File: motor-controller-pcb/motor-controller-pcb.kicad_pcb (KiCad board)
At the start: 2 copper layers, 90 x 65 mm, 15 parts, among them J1 Conn_01x06_Pin, J2 Conn_01x06_Pin, J3 Conn_01x06_Pin, J4 Conn_01x06_Pin, J5 Conn_01x04_Pin, J6 Conn_01x04_Pin, M1 Conn_01x02_Pin, M2 Conn_01x02_Pin, M3 Conn_01x02_Pin, M4 Conn_01x02_Pin

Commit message: fix: change pcb footprint to jst ph
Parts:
- J1, J2, J3, J4: footprint Connector_JST:JST_SH_BM06B-SRSS-TB_1x06-1MP_P1.00mm_Vertical -> Connector_JST:JST_PH_B6B-PH-K_1x06_P2.00mm_Vertical
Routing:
- net +5V: track 146.9 -> 0.00 mm
- net /Encoder 2A: track 79.7 -> 1.22 mm
- net /Encoder 1B: track 68.7 -> 1.13 mm, vias 2 -> 0
- net /Encoder 3B: track 50.0 -> 0.00 mm
- net GND: track 148.4 -> 100.4 mm, vias 3 -> 0
- net /Encoder 2B: track 47.4 -> 0.00 mm, vias 1 -> 0
- net /Encoder 3A: track 45.5 -> 0.00 mm
- net /Encoder 1A: track 45.4 -> 0.00 mm, vias 1 -> 0
- net Net-(J4-Pin_1): track 33.7 -> 0.00 mm
- net /Encoder 4B: track 33.7 -> 0.00 mm, vias 1 -> 0
- net /Encoder 4A: track 33.2 -> 0.00 mm, vias 1 -> 0
- net Net-(J2-Pin_1): track 29.8 -> 0.00 mm, vias 2 -> 0
- net Net-(J1-Pin_6): track 28.3 -> 0.00 mm, vias 1 -> 0
- net Net-(J4-Pin_6): track 22.0 -> 0.00 mm
- net Net-(J2-Pin_6): track 19.4 -> 0.00 mm
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
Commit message: feat: pcb layout
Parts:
- removed M1, M2, M3, M4: Conn_01x02_Pin, Connector_PinHeader_2.54mm:PinHeader_1x02_P2.54mm_Vertical
- removed REF** (x4): MountingHole_3.2mm_M3, MountingHole:MountingHole_3.2mm_M3
- added C1: 470uF, Capacitor_THT:CP_Radial_D8.0mm_P3.50mm, F.Cu at (115.6, 129.5)
- added C2: 100nF, Capacitor_SMD:C_0805_2012Metric, F.Cu at (146.1, 78.7)
- added C3: 100nF, Capacitor_SMD:C_0805_2012Metric, F.Cu at (146.1, 39.4)
- added C4: 100nF, Capacitor_SMD:C_0805_2012Metric, F.Cu at (180.3, 59.7)
- added F1: Fuse, Fuse:Fuseholder_Clip-5x20mm_Littelfuse_100_Inline_P20.50x4.60mm_D1.30mm_Horizontal, F.Cu at (152.4, 105.4)
- added J10: 3V3, Connector_PinHeader_2.54mm:PinHeader_1x10_P2.54mm_Vertical, F.Cu at (196.7, 67.3)
- added J11: Conn_01x05_Pin, Connector_PinHeader_2.54mm:PinHeader_1x05_P2.54mm_Vertical, F.Cu at (195.4, 97.8)
- added J7: GND, Connector_PinHeader_2.54mm:PinHeader_1x10_P2.54mm_Vertical, F.Cu at (182.9, 67.3)
- added J8: 5V, Connector_PinHeader_2.54mm:PinHeader_1x10_P2.54mm_Vertical, F.Cu at (187.5, 67.3)
- added J9: V_Batt, Connector_PinHeader_2.54mm:PinHeader_1x10_P2.54mm_Vertical, F.Cu at (192.1, 67.3)
- added SW1: Battery Switch, Connector_Wire:SolderWire-2sqmm_1x02_P7.8mm_D2mm_OD3.9mm_Relief2x, F.Cu at (125.7, 140.0)
- added TP1: 5V TestPoint, TestPoint:TestPoint_Pad_1.5x1.5mm, F.Cu at (181.6, 106.7)
- added TP2: GND TestPoint, TestPoint:TestPoint_Pad_1.5x1.5mm, F.Cu at (186.7, 106.7)
- added TP3: V_Batt Test Point, TestPoint:TestPoint_Pad_1.5x1.5mm, F.Cu at (191.5, 106.7)
- added TP4: 3V3 Test Point, TestPoint:TestPoint_Pad_1.5x1.5mm, F.Cu at (196.8, 106.7)
- added U1: ~, robocup-library:DRI044, F.Cu at (137.2, 88.9)
- added U2: ~, robocup-library:DRI044, F.Cu at (137.2, 49.5)
- added U3: ~, robocup-library:DRI044, F.Cu at (189.2, 49.5)
- J1: value Conn_01x06_Pin -> Motor 1
- J2: value Conn_01x06_Pin -> Motor 2
- J3: value Conn_01x06_Pin -> Motor 3
- J4: value Conn_01x06_Pin -> Motor 4
- J5: value Conn_01x04_Pin -> Dribbler Motor; footprint Connector_PinHeader_2.54mm:PinHeader_1x04_P2.54mm_Vertical -> Connector_JST:JST_PH_B6B-PH-K_1x06_P2.00mm_Vertical
- J6: value Conn_01x04_Pin -> Battery Connector; footprint Connector_PinHeader_2.54mm:PinHeader_1x04_P2.54mm_Vertical -> Connector_Wire:SolderWire-2sqmm_1x02_P7.8mm_D2mm_OD3.9mm_Relief2x
- moved J3 115.4 mm to (212.1, 43.3), turned to -90 degrees
- moved J2 79.2 mm to (115.6, 53.2), turned to 90 degrees
- moved J6 47.2 mm to (125.2, 124.8), turned to 90 degrees
- moved J5 38.4 mm to (131.2, 102.9)
- moved J1 24.5 mm to (116.3, 93.9)
- moved J4 23.3 mm to (213.4, 82.5)
- moved A1 17.8 mm to (162.6, 67.7)
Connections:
- A1 pad 1: unconnected-(A1-GPIO0-Pad1) -> /DIR_DRIB
- A1 pad 10: Net-(A1-GPIO7) -> /PWM3
- A1 pad 11: Net-(A1-GPIO8) -> /PWM4
- A1 pad 12: Net-(A1-GPIO9) -> /DIR4
- A1 pad 14: unconnected-(A1-GPIO10-Pad14)_1 -> /GPIO10
- A1 pad 2: unconnected-(A1-GPIO1-Pad2)_1 -> /PWM_DRIB
- A1 pad 20: unconnected-(A1-GPIO15-Pad20) -> /GPIO15
- A1 pad 21: unconnected-(A1-GPIO16-Pad21)_1 -> /GPIO16
- A1 pad 22: unconnected-(A1-GPIO17-Pad22) -> /GPIO17
- A1 pad 24: unconnected-(A1-GPIO18-Pad24)_1 -> /GPIO18
- A1 pad 36: unconnected-(A1-3V3-Pad36)_1 -> +3V3
- A1 pad 4: Net-(A1-GPIO2) -> /DIR1
- A1 pad 5: Net-(A1-GPIO3) -> /PWM1
- A1 pad 6: Net-(A1-GPIO4) -> /PWM2
- A1 pad 7: Net-(A1-GPIO5) -> /DIR2
- A1 pad 9: Net-(A1-GPIO6) -> /DIR3
- J5 pad 1: Net-(A1-GPIO2) -> Net-(J5-Pin_1)
- J5 pad 2: Net-(A1-GPIO3) -> unconnected-(J5-Pin_2-Pad2)
- J5 pad 3: Net-(A1-GPIO4) -> unconnected-(J5-Pin_3-Pad3)
- J5 pad 4: Net-(A1-GPIO5) -> unconnected-(J5-Pin_4-Pad4)
- J6 pad 1: Net-(A1-GPIO6) -> Net-(J6-Pin_1)
- J6 pad 2: Net-(A1-GPIO7) -> GND
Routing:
- net GND: track 100.4 -> 0.00 mm
- net Net-(A1-GPIO2): track 9.42 -> 0.00 mm
- net Net-(A1-GPIO9): track 8.89 -> 0.00 mm
- net Net-(A1-GPIO6): track 8.89 -> 0.00 mm
- net Net-(A1-GPIO5): track 8.62 -> 0.00 mm
- net Net-(A1-GPIO4): track 8.62 -> 0.00 mm
- net Net-(A1-GPIO3): track 8.62 -> 0.00 mm
- net Net-(A1-GPIO8): track 8.09 -> 0.00 mm
- net Net-(A1-GPIO7): track 8.09 -> 0.00 mm
- net /Encoder 2A: track 1.22 -> 0.00 mm
- net /Encoder 1B: track 1.13 -> 0.00 mm
- removed copper zone on B.Cu, net GND
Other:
- board size 90 x 65 mm -> 110.5 x 110.5 mm
- board text added: "High Scorers 2026"
- board text added: "Motor Controller Rev2"
- board text added: "PCB design by Hamzah Ahmed"
- board text removed: "Robocup 2025 SBHS PCB by Hamzah Ahmed"

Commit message: feat: final
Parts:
- added J12: V_Batt, TerminalBlock:TerminalBlock_MaiXu_MX126-5.0-02P_1x02_P5.00mm, F.Cu at (116.8, 141.0)
- added REF**: MountingHole_3.2mm_M3, MountingHole:MountingHole_3.2mm_M3, F.Cu at (215.0, 150.0)
- added REF**: MountingHole_3.2mm_M3, MountingHole:MountingHole_3.2mm_M3, F.Cu at (110.0, 150.0)
- added REF**: MountingHole_3.2mm_M3, MountingHole:MountingHole_3.2mm_M3, F.Cu at (215.0, 35.0)
- added REF**: MountingHole_3.2mm_M3, MountingHole:MountingHole_3.2mm_M3, F.Cu at (110.0, 35.0)
- J1, J2, J3, J4: moved to B.Cu
- moved SW1 7.69 mm to (126.0, 147.7)
- moved C4 1.27 mm to (180.3, 61.0)
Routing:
- net +5V: track 0.00 -> 365.8 mm, vias 0 -> 1
- net GND: track 0.00 -> 290.3 mm, vias 0 -> 4
- net +BATT: track 0.00 -> 235.1 mm, vias 0 -> 3
- net /PWM_DRIB: track 0.00 -> 127.8 mm
- net /Encoder 3B: track 0.00 -> 106.2 mm
- net /Encoder 3A: track 0.00 -> 82.2 mm
- net /Encoder 2A: track 0.00 -> 79.1 mm
- net /Encoder 2B: track 0.00 -> 75.2 mm, vias 0 -> 1
- net /DIR_DRIB: track 0.00 -> 74.6 mm
- net +3V3: track 0.00 -> 70.3 mm
- net /Encoder 4A: track 0.00 -> 64.6 mm
- net Net-(SW1-A): track 0.00 -> 60.3 mm
- net /Encoder 4B: track 0.00 -> 60.3 mm
- net /DIR4: track 0.00 -> 60.1 mm
- net /PWM4: track 0.00 -> 52.1 mm
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- added copper zone on B.Cu, net GND
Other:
- board size 110.5 x 110.5 mm -> 117 x 126.9 mm

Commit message: feat: pcb prettification
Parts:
- J5: moved to B.Cu
- U1, U2, U3: footprint robocup-library:DRI044 -> robocup-library:DRI0044
- moved J5 9.56 mm to (140.7, 103.1), turned to 180 degrees
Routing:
- net Net-(J5-Pin_1): track 8.82 -> 21.4 mm
- net Net-(J5-Pin_6): track 21.0 -> 11.4 mm
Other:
- outline, holes or cut-outs redrawn
- board text added: "+"
- board text added: "-"
- board text added: "3.3V"
- board text added: "5V"
- board text added: "Batt"
- board text added: "GND"
- board text added: "GPIO10"
- board text added: "GPIO15"
- board text added: "GPIO16"
- board text added: "GPIO17"
- board text added: "GPIO18"

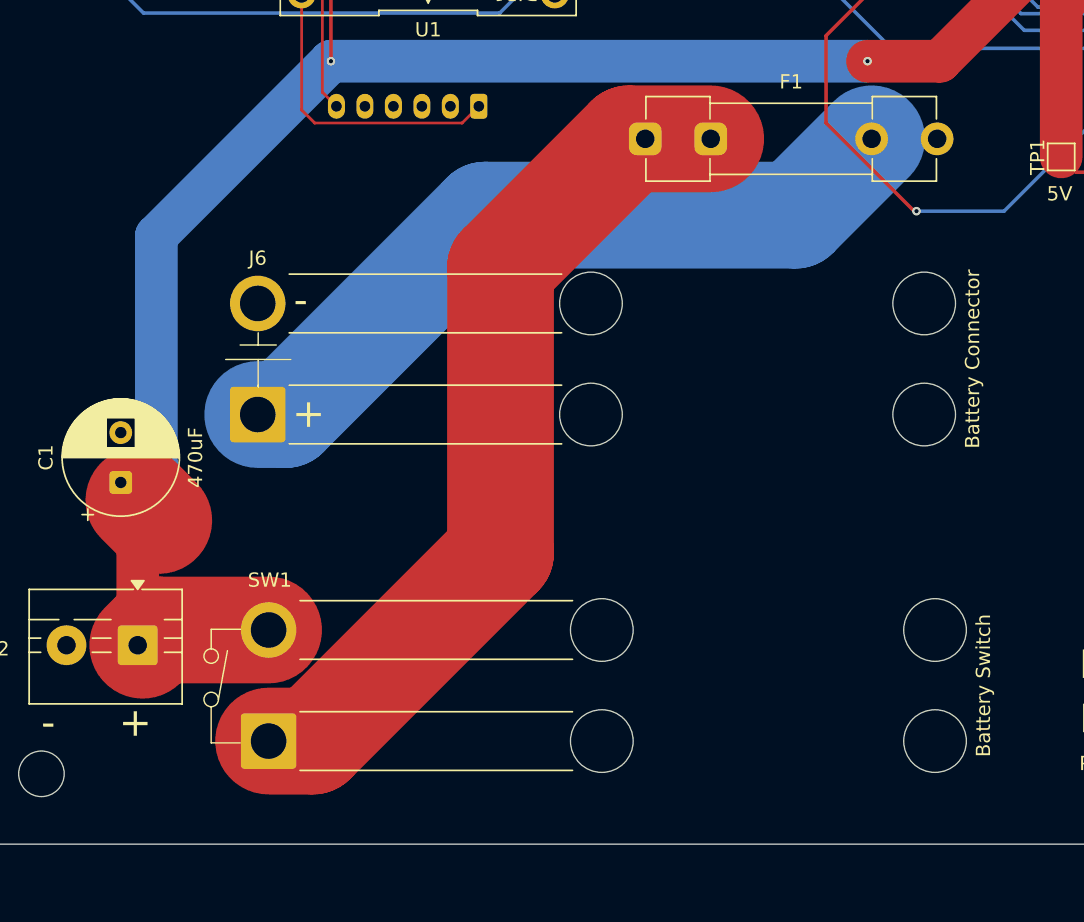
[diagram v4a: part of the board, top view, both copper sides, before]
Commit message: fix: make wire strain relief holes large enough
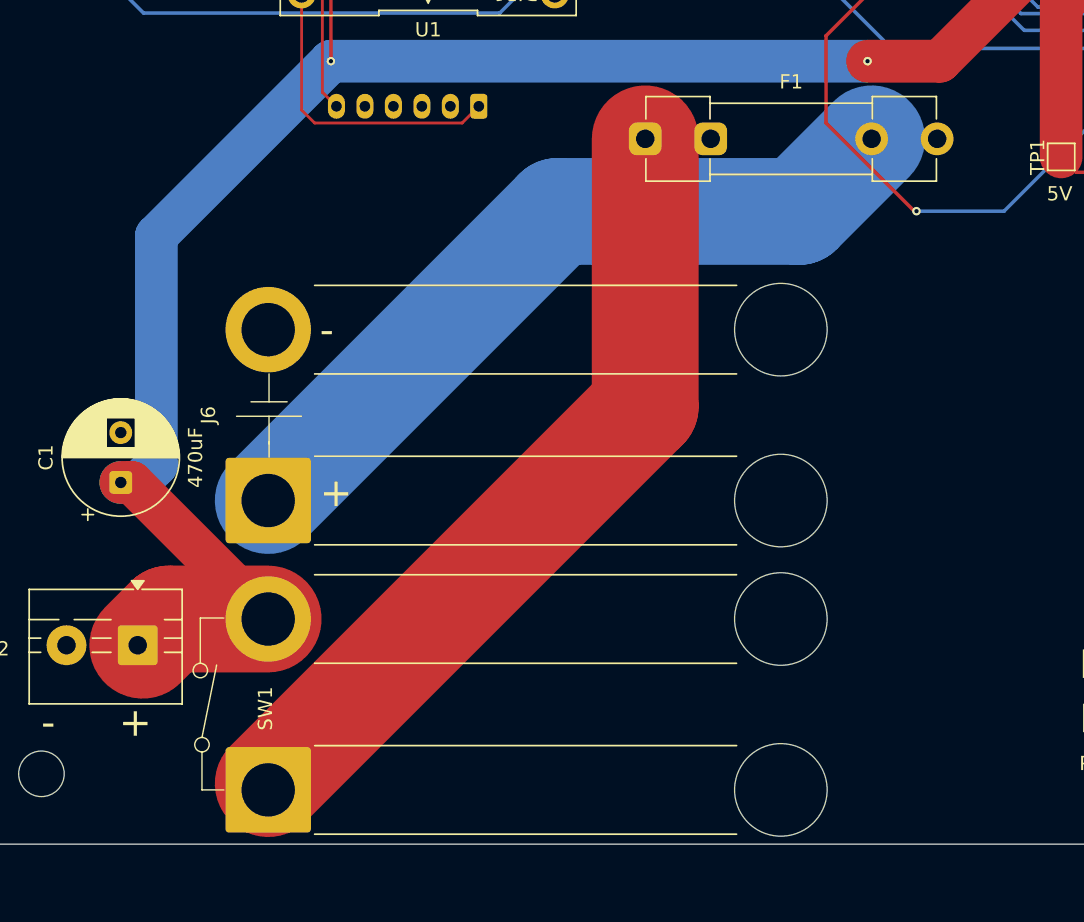
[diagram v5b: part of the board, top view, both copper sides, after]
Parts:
- J6, SW1: footprint Connector_Wire:SolderWire-2sqmm_1x02_P7.8mm_D2mm_OD3.9mm_Relief2x -> Connector_Wire:SolderWire-4sqmm_1x02_P12mm_D3mm_OD6mm_Relief
- moved J6 6.08 mm to (125.9, 130.8)
- moved SW1 3.43 mm to (125.9, 151.1)
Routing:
- net Net-(SW1-A): track 60.3 -> 56.2 mm
- net +BATT: track 235.1 -> 238.4 mm
- net Net-(J6-Pin_1): track 51.1 -> 52.9 mm
